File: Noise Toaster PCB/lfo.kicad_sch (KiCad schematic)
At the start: 15 parts, among them U2 LM324

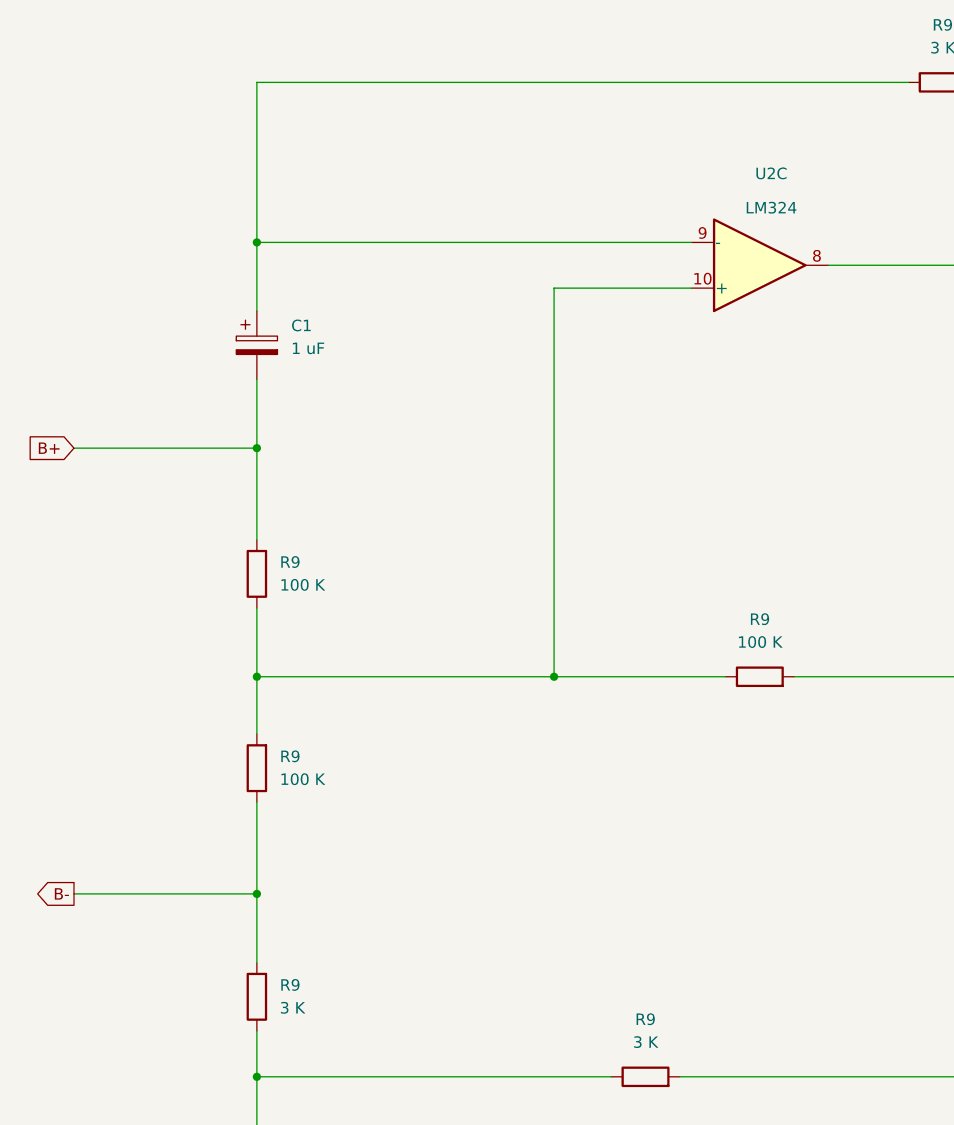
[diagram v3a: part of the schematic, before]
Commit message: wireing and components have been checked
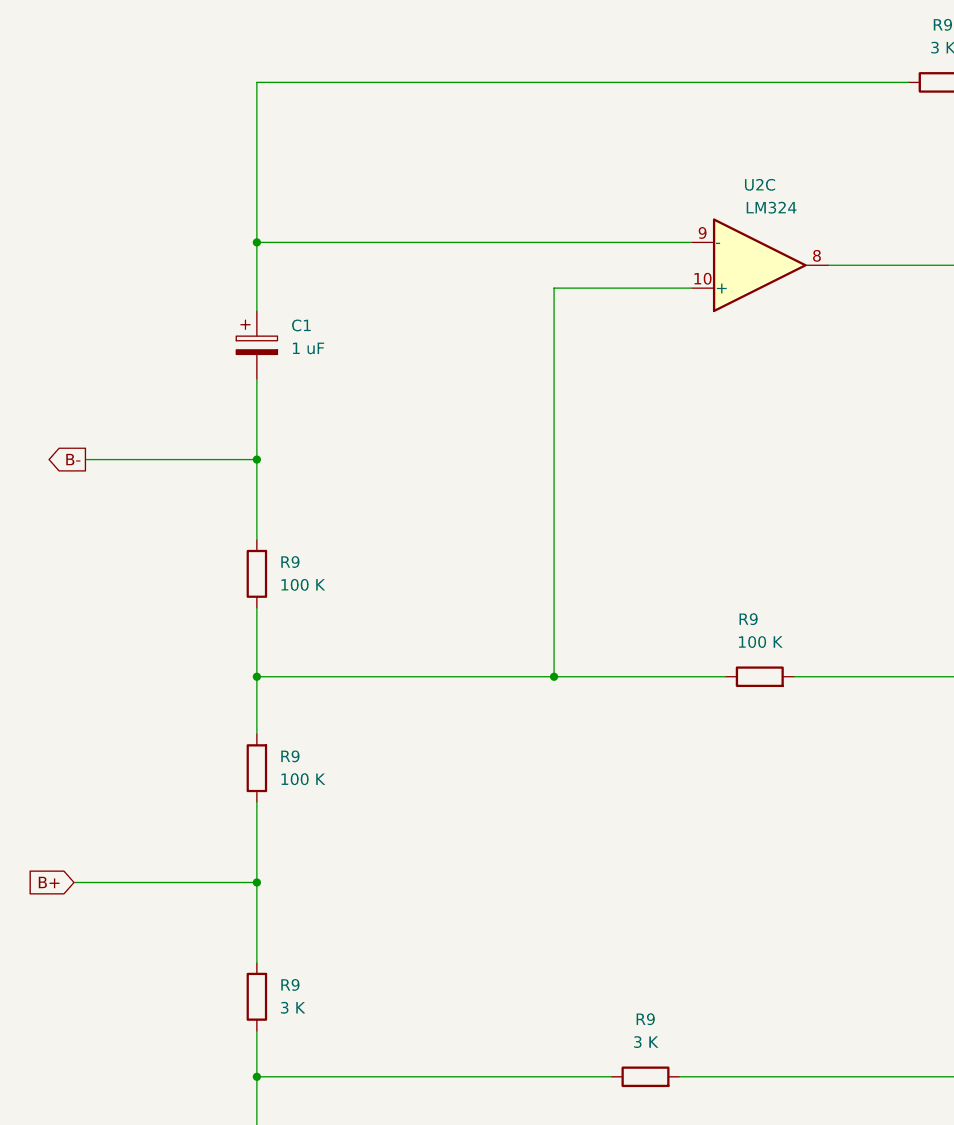
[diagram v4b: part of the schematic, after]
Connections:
- net B+: now also R9.1, R9.2; no longer C1.2, R9.2
- net B-: now also C1.2, R9.2; no longer R9.1, R9.2
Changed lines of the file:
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@@
     (comment 3 "Music From Outer Space LLC")
   )
+  (junction (at 63.5 130.81) (diameter 0) (color 0 0 0 0)
+  )
   (junction (at 152.4 62.23) (diameter 0) (color 0 0 0 0)
   )
@@
   (junction (at 222.25 62.23) (diameter 0) (color 0 0 0 0)
   )
+  (junction (at 63.5 83.82) (diameter 0) (color 0 0 0 0)
+  )
   (junction (at 63.5 59.69) (diameter 0) (color 0 0 0 0)
   )
@@
   (junction (at 223.52 41.91) (diameter 0) (color 0 0 0 0)
   )
-  (junction (at 63.5 82.55) (diameter 0) (color 0 0 0 0)
-  )
   (junction (at 63.5 152.4) (diameter 0) (color 0 0 0 0)
   )
   (junction (at 63.5 107.95) (diameter 0) (color 0 0 0 0)
   )
-  (junction (at 63.5 132.08) (diameter 0) (color 0 0 0 0)
-  )
   (junction (at 152.4 107.95) (diameter 0) (color 0 0 0 0)
   )
@@
     (stroke (width 0) (type default))
   )
+  (wire (pts (xy 43.18 130.81) (xy 63.5 130.81))
+    (stroke (width 0) (type default))
+  )
   (wire (pts (xy 123.19 107.95) (xy 152.4 107.95))
     (stroke (width 0) (type default))
@@
     (stroke (width 0) (type default))
   )
-  (wire (pts (xy 63.5 132.08) (xy 63.5 139.7))
+  (wire (pts (xy 63.5 83.82) (xy 63.5 92.71))
     (stroke (width 0) (type default))
   )
@@
     (stroke (width 0) (type default))
   )
-  (wire (pts (xy 63.5 82.55) (xy 63.5 92.71))
+  (wire (pts (xy 63.5 74.93) (xy 63.5 83.82))
     (stroke (width 0) (type default))
   )
@@
     (stroke (width 0) (type default))
   )
+  (wire (pts (xy 63.5 121.92) (xy 63.5 130.81))
+    (stroke (width 0) (type default))
+  )
   (wire (pts (xy 96.52 107.95) (xy 115.57 107.95))
     (stroke (width 0) (type default))
   )
-  (wire (pts (xy 43.18 132.08) (xy 63.5 132.08))
+  (wire (pts (xy 44.45 83.82) (xy 63.5 83.82))
     (stroke (width 0) (type default))
   )
@@
     (stroke (width 0) (type default))
   )
-  (wire (pts (xy 43.18 82.55) (xy 63.5 82.55))
-    (stroke (width 0) (type default))
-  )
   (wire (pts (xy 152.4 62.23) (xy 152.4 107.95))
     (stroke (width 0) (type default))
@@
     (stroke (width 0) (type default))
   )
-  (wire (pts (xy 63.5 74.93) (xy 63.5 82.55))
-    (stroke (width 0) (type default))
-  )
-  (wire (pts (xy 63.5 121.92) (xy 63.5 132.08))
+  (wire (pts (xy 63.5 130.81) (xy 63.5 139.7))
     (stroke (width 0) (type default))
   )
@@
     (stroke (width 0) (type default))
   )
-  (global_label "B-" (shape output) (at 43.18 132.08 180) (fields_autoplaced)
+  (global_label "B-" (shape output) (at 44.45 83.82 180) (fields_autoplaced)
     (effects (font (size 1.27 1.27)) (justify right))
-    (property "Intersheetrefs" "${INTERSHEET_REFS}" (at 37.3524 132.08 0)
+    (property "Intersheetrefs" "${INTERSHEET_REFS}" (at 38.6224 83.82 0)
       (effects (font (size 1.27 1.27)) (justify right) hide)
     )
@@
     )
   )
-  (global_label "B+" (shape input) (at 43.18 82.55 180) (fields_autoplaced)
+  (global_label "B+" (shape input) (at 43.18 130.81 180) (fields_autoplaced)
     (effects (font (size 1.27 1.27)) (justify right))
-    (property "Intersheetrefs" "${INTERSHEET_REFS}" (at 37.3524 82.55 0)
+    (property "Intersheetrefs" "${INTERSHEET_REFS}" (at 37.3524 130.81 0)
       (effects (font (size 1.27 1.27)) (justify right) hide)
     )
@@
   )
   (symbol (lib_id "Device:R") (at 119.38 107.95 90) (unit 1)
-    (in_bom yes) (on_board yes) (dnp no) (fields_autoplaced)
-    (property "Reference" "R9" (at 119.38 101.6 90)
+    (in_bom yes) (on_board yes) (dnp no)
+    (property "Reference" "R9" (at 118.11 101.6 90)
       (effects (font (size 1.27 1.27)))
     )
@@
   (symbol (lib_id "Amplifier_Operational:LM324") (at 119.38 62.23 0) (mirror x) (unit 3)
     (in_bom yes) (on_board yes) (dnp no)
-    (property "Reference" "U2" (at 120.65 52.07 0)
-      (effects (font (size 1.27 1.27)))
-    )
+    (property "Reference" "U2" (at 119.38 53.34 0)
+      (effects (font (size 1.27 1.27)))
+    )

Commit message: applied footprints
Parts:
- C1: footprint (none) -> Capacitor_THT:CP_Radial_D5.0mm_P2.00mm
- C1: footprint (none) -> Capacitor_THT:CP_Radial_D14.0mm_P5.00mm
- R9: footprint (none) -> Resistor_THT:R_Axial_DIN0207_L6.3mm_D2.5mm_P10.16mm_Horizontal
- U2: footprint (none) -> Package_DIP:DIP-14_W7.62mm_Socket
- X4: footprint (none) -> Connector_PinHeader_1.00mm:PinHeader_1x01_P1.00mm_Vertical
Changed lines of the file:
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@@
       (effects (font (size 1.27 1.27)))
     )
-    (property "Footprint" "" (at 106.68 154.178 90)
+    (property "Footprint" "Resistor_THT:R_Axial_DIN0207_L6.3mm_D2.5mm_P10.16mm_Horizontal" (at 106.68 154.178 90)
       (effects (font (size 1.27 1.27)) hide)
     )
@@
       (effects (font (size 1.27 1.27)) (justify right))
     )
-    (property "Footprint" "" (at 65.278 118.11 90)
+    (property "Footprint" "Resistor_THT:R_Axial_DIN0207_L6.3mm_D2.5mm_P10.16mm_Horizontal" (at 65.278 118.11 90)
       (effects (font (size 1.27 1.27)) hide)
     )
@@
       (effects (font (size 1.27 1.27)))
     )
-    (property "Footprint" "" (at 233.68 107.95 0)
+    (property "Footprint" "Connector_PinHeader_1.00mm:PinHeader_1x01_P1.00mm_Vertical" (at 233.68 107.95 0)
       (effects (font (size 1.27 1.27)) hide)
     )
@@
       (effects (font (size 1.27 1.27)) (justify right))
     )
-    (property "Footprint" "" (at 65.278 96.52 90)
+    (property "Footprint" "Resistor_THT:R_Axial_DIN0207_L6.3mm_D2.5mm_P10.16mm_Horizontal" (at 65.278 96.52 90)
       (effects (font (size 1.27 1.27)) hide)
     )
@@
       (effects (font (size 1.27 1.27)))
     )
-    (property "Footprint" "" (at 119.38 109.728 90)
+    (property "Footprint" "Resistor_THT:R_Axial_DIN0207_L6.3mm_D2.5mm_P10.16mm_Horizontal" (at 119.38 109.728 90)
       (effects (font (size 1.27 1.27)) hide)
     )
@@
       (effects (font (size 1.27 1.27)))
     )
-    (property "Footprint" "" (at 232.41 62.23 0)
+    (property "Footprint" "Connector_PinHeader_1.00mm:PinHeader_1x01_P1.00mm_Vertical" (at 232.41 62.23 0)
       (effects (font (size 1.27 1.27)) hide)
     )
@@
       (effects (font (size 1.27 1.27)) (justify left))
     )
-    (property "Footprint" "" (at 204.1652 134.62 0)
+    (property "Footprint" "Capacitor_THT:CP_Radial_D5.0mm_P2.00mm" (at 204.1652 134.62 0)
       (effects (font (size 1.27 1.27)) hide)
     )
@@
       (effects (font (size 1.27 1.27)))
     )
-    (property "Footprint" "" (at 223.52 25.4 0)
+    (property "Footprint" "Connector_PinHeader_1.00mm:PinHeader_1x01_P1.00mm_Vertical" (at 223.52 25.4 0)
       (effects (font (size 1.27 1.27)) hide)
     )
@@
       (effects (font (size 1.27 1.27)))
     )
-    (property "Footprint" "" (at 154.94 152.4 0)
+    (property "Footprint" "Connector_PinHeader_1.00mm:PinHeader_1x01_P1.00mm_Vertical" (at 154.94 152.4 0)
       (effects (font (size 1.27 1.27)) hide)
     )
@@
       (effects (font (size 1.27 1.27)))
     )
-    (property "Footprint" "" (at 139.7 43.688 90)
+    (property "Footprint" "Resistor_THT:R_Axial_DIN0207_L6.3mm_D2.5mm_P10.16mm_Horizontal" (at 139.7 43.688 90)
       (effects (font (size 1.27 1.27)) hide)
     )
@@
       (effects (font (size 1.27 1.27)) (justify left))
     )
-    (property "Footprint" "" (at 64.4652 168.91 0)
+    (property "Footprint" "Capacitor_THT:CP_Radial_D14.0mm_P5.00mm" (at 64.4652 168.91 0)
       (effects (font (size 1.27 1.27)) hide)
     )
@@
       (effects (font (size 1.27 1.27)) (justify right))
     )
-    (property "Footprint" "" (at 65.278 143.51 90)
+    (property "Footprint" "Resistor_THT:R_Axial_DIN0207_L6.3mm_D2.5mm_P10.16mm_Horizontal" (at 65.278 143.51 90)
       (effects (font (size 1.27 1.27)) hide)
     )
@@
       (effects (font (size 1.27 1.27)) (justify left))
     )
-    (property "Footprint" "" (at 64.4652 74.93 0)
+    (property "Footprint" "Capacitor_THT:CP_Radial_D5.0mm_P2.00mm" (at 64.4652 74.93 0)
       (effects (font (size 1.27 1.27)) hide)
     )
@@
       (effects (font (size 1.27 1.27)))
     )
-    (property "Footprint" "" (at 177.8 109.728 90)
+    (property "Footprint" "Resistor_THT:R_Axial_DIN0207_L6.3mm_D2.5mm_P10.16mm_Horizontal" (at 177.8 109.728 90)
       (effects (font (size 1.27 1.27)) hide)
     )
@@
       (effects (font (size 1.27 1.27)))
     )
-    (property "Footprint" "" (at 118.11 64.77 0)
-      (effects (font (size 1.27 1.27)) hide)
-    )
+    (property "Footprint" "Package_DIP:DIP-14_W7.62mm_Socket" (at 118.11 64.77 0)
+      (effects (font (size 1.27 1.27)) hide)
+    )

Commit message: placed pards of the pcb properly
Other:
- company: http://musicfromouterspace.com/analogsynth_new/NOISETOASTER/NOISETOASTER.php -> Music From Outer Space LLC
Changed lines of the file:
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@@
     (title "Low Frequency Oscillator")
     (rev "0.5")
-    (company "http://musicfromouterspace.com/analogsynth_new/NOISETOASTER/NOISETOASTER.php")
+    (company "Music From Outer Space LLC")
     (comment 1 "Licence: CC-BY-NC-SA")
     (comment 2 "Original Design by Ray Wilson")
-    (comment 3 "Music From Outer Space LLC")
+    (comment 3 "http://musicfromouterspace.com/analogsynth_new/NOISETOASTER/NOISETOASTER.php")
   )
   (junction (at 63.5 130.81) (diameter 0) (color 0 0 0 0)

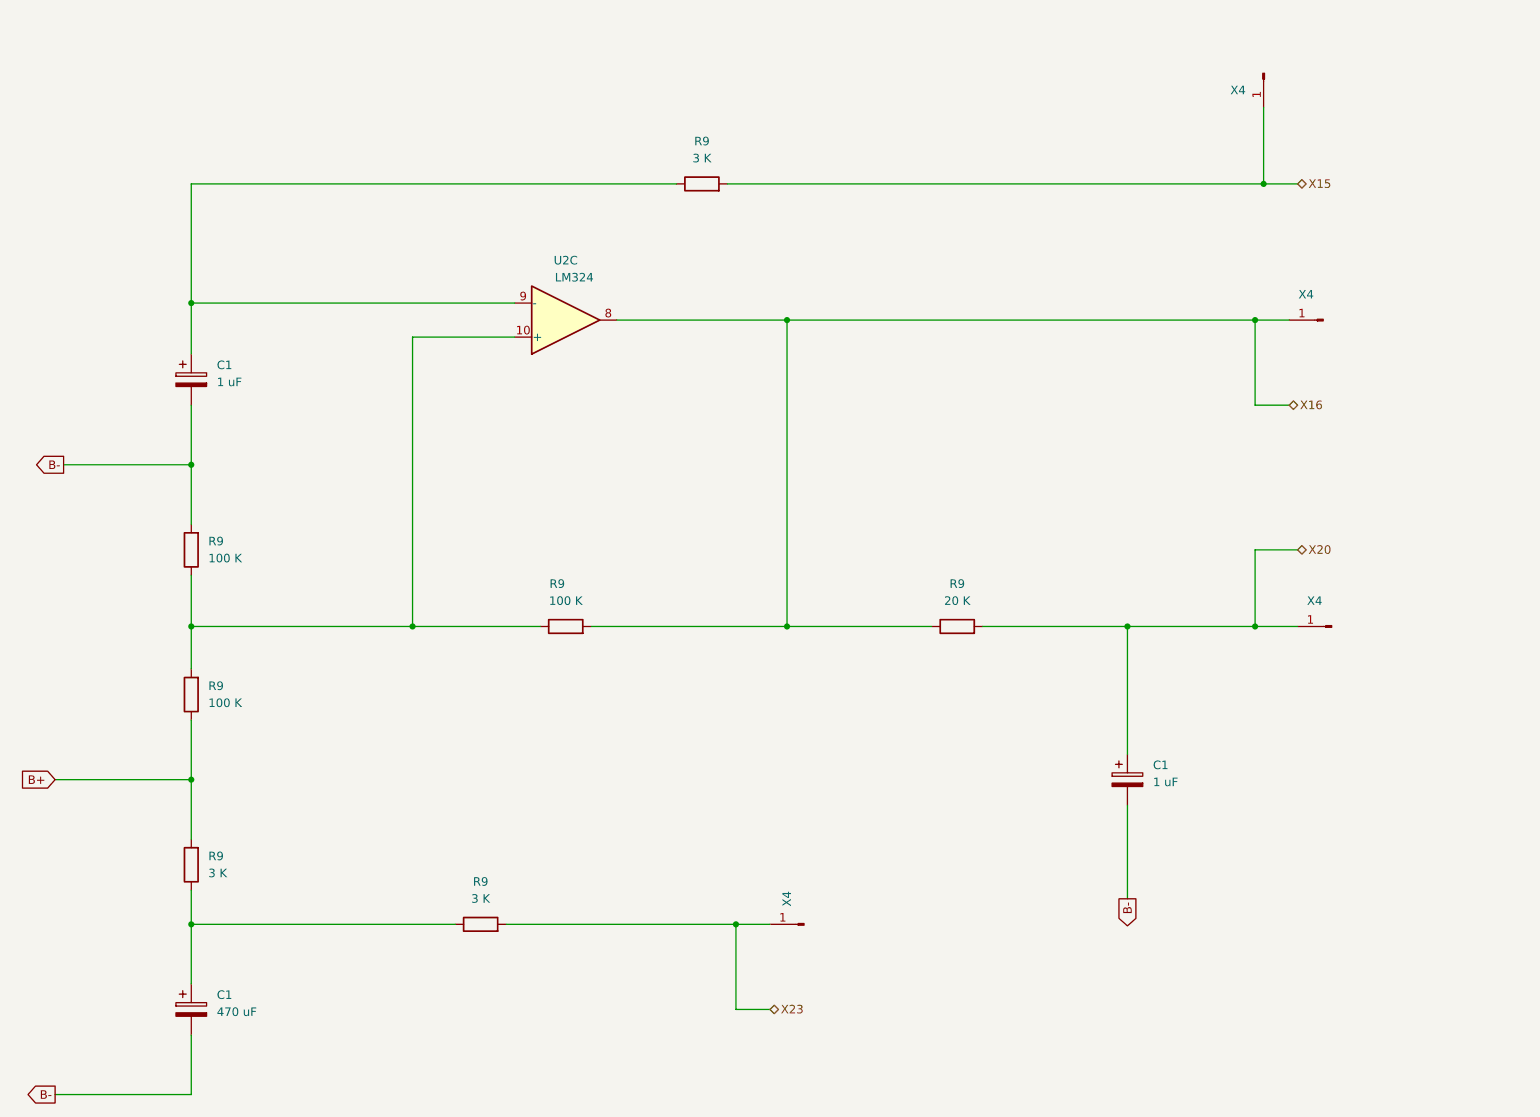
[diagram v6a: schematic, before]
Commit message: changed header pins to groups
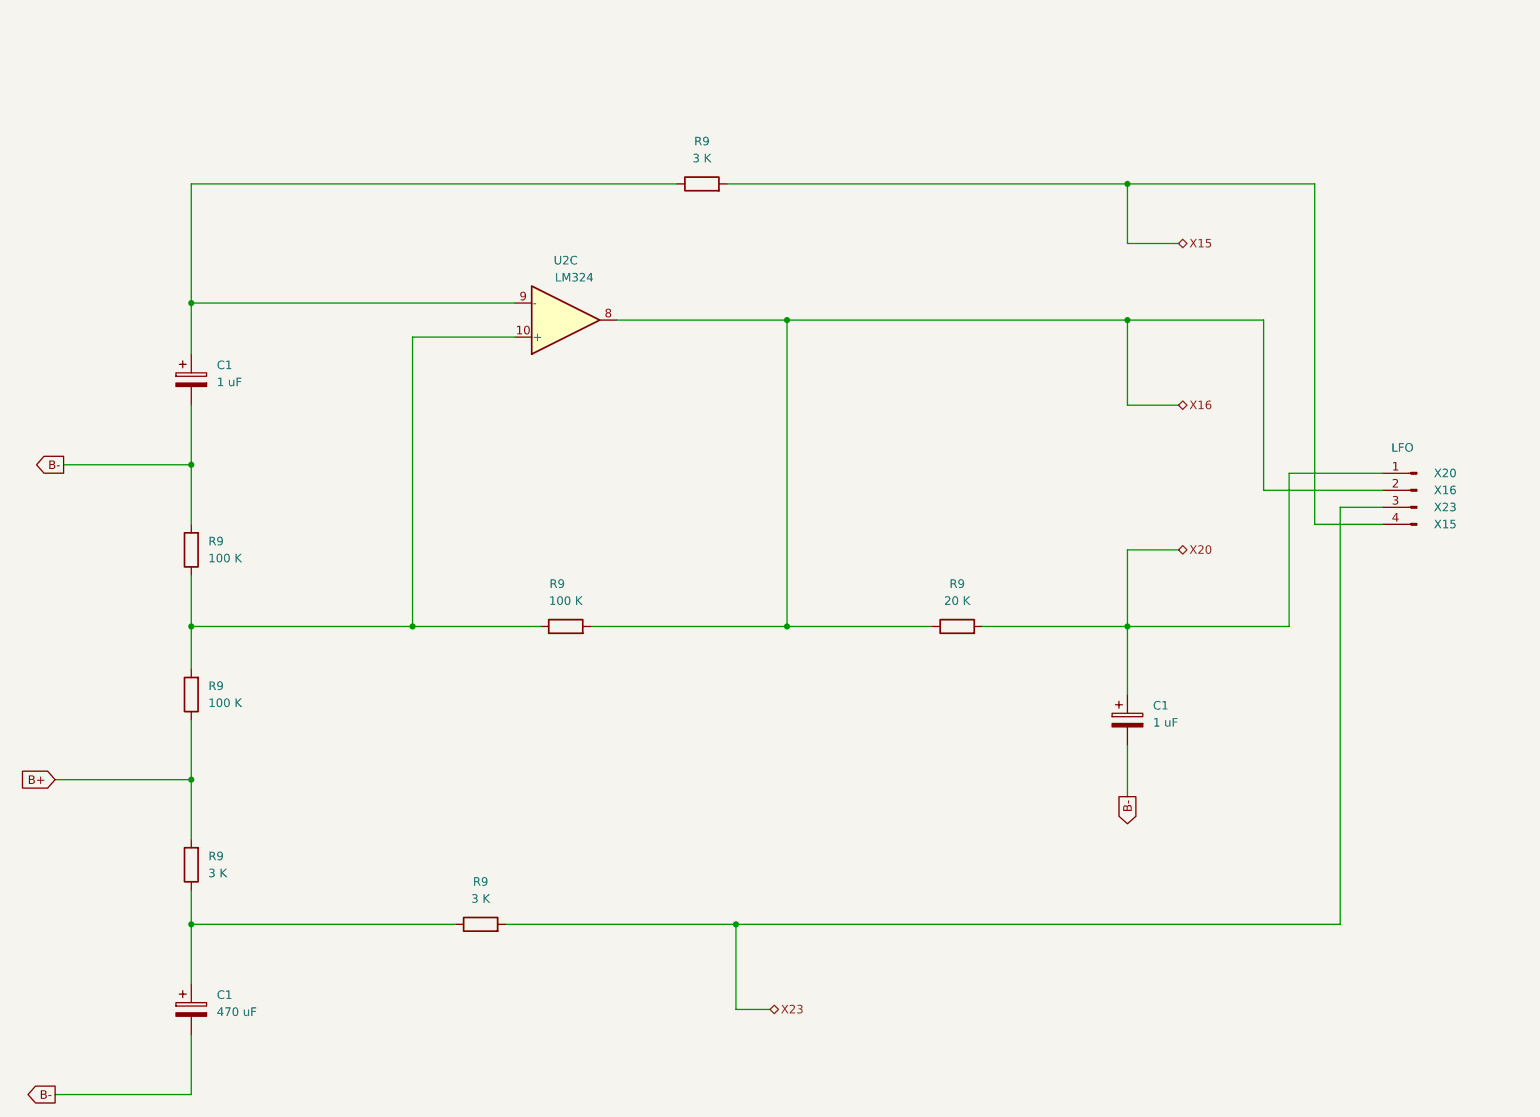
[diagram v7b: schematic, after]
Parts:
- removed X4 (x4): ~, Connector_PinHeader_1.00mm:PinHeader_1x01_P1.00mm_Vertical, symbol Connector:Conn_01x01_Pin
- added J4: LFO, Connector_PinHeader_2.00mm:PinHeader_1x04_P2.00mm_Vertical, symbol Connector:Conn_01x04_Pin
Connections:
- net X15: now also J4.4 (Pin_4)
- net X16: now also J4.2 (Pin_2)
- net X20: now also J4.1 (Pin_1)
- net X23: now also J4.3 (Pin_3)
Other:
- moved on the sheet: C1
